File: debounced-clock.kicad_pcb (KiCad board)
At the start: 2 copper layers, 74.9 x 40.6 mm, 31 parts, among them P1 POWER, P2 POT, P3 STEP, P4 SWITCH, P5 HALT, P6 LED, P7 POWER, U1 NE555, U2 7400, U3 7400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

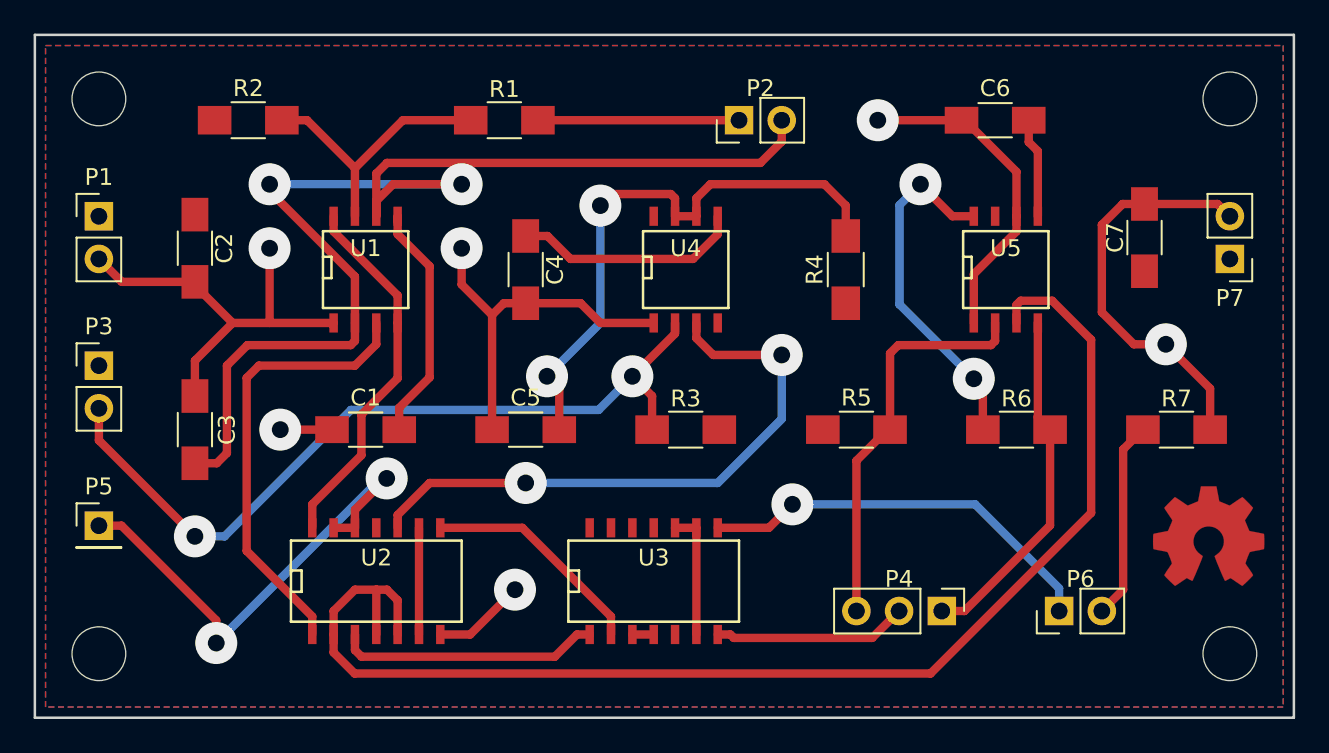
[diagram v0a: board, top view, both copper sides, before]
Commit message: Schematics/PCB fix, Via size change, OSH logo moved to silk layer
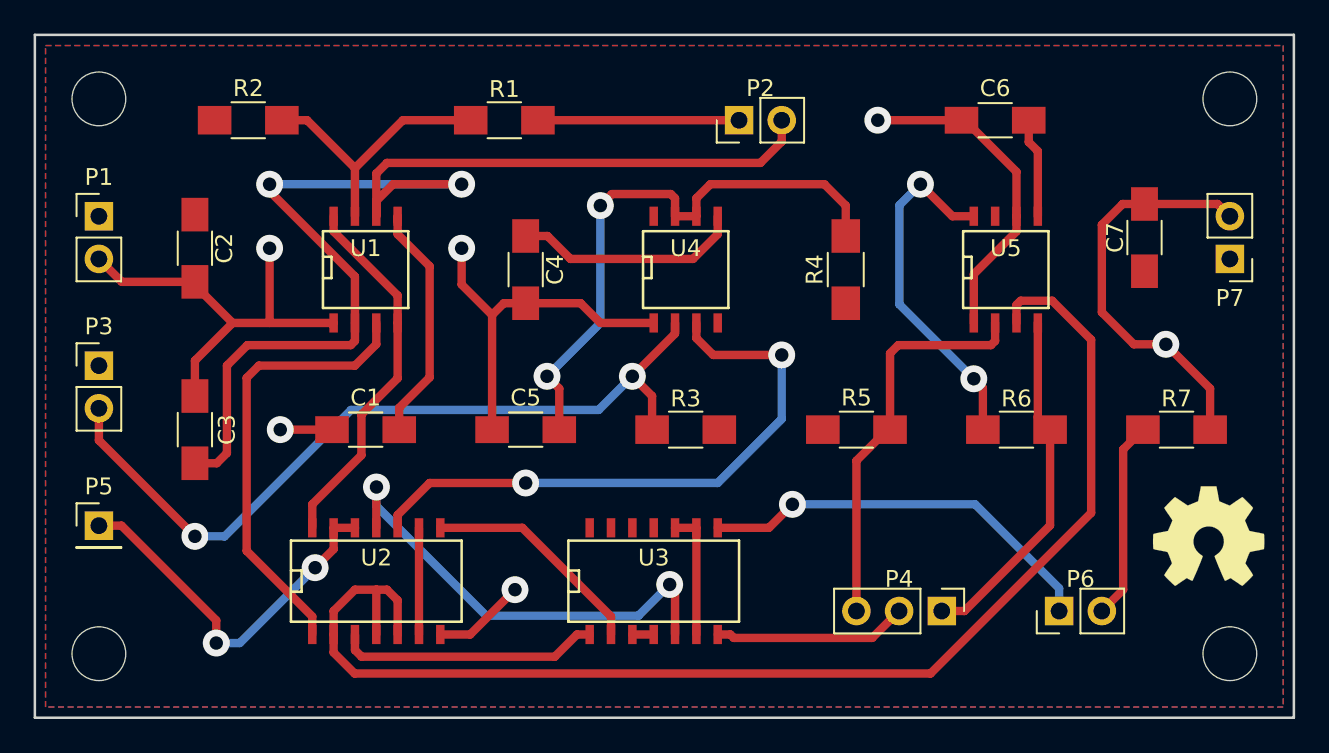
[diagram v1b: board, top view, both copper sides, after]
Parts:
- REF***: footprint Symbols:OSHW-Symbol_6.7x6mm_Copper -> Symbol:OSHW-Symbol_6.7x6mm_SilkScreen
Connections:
- U3 pad 5: Net-(U3-Pad5) -> Net-(U2-Pad11)
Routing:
- net Net-(U2-Pad11): track 0.00 -> 27.6 mm, vias 0 -> 2
- net HALT: track 29.9 -> 22.5 mm
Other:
- net class Default: via_dia 2.5 -> 1.6; via_drill 1 -> 0.8
